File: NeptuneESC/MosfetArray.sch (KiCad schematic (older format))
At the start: 24 parts, among them Q1 Q_NPN_BCE, Q2 Q_NPN_BCE, Q3 Q_NPN_BCE

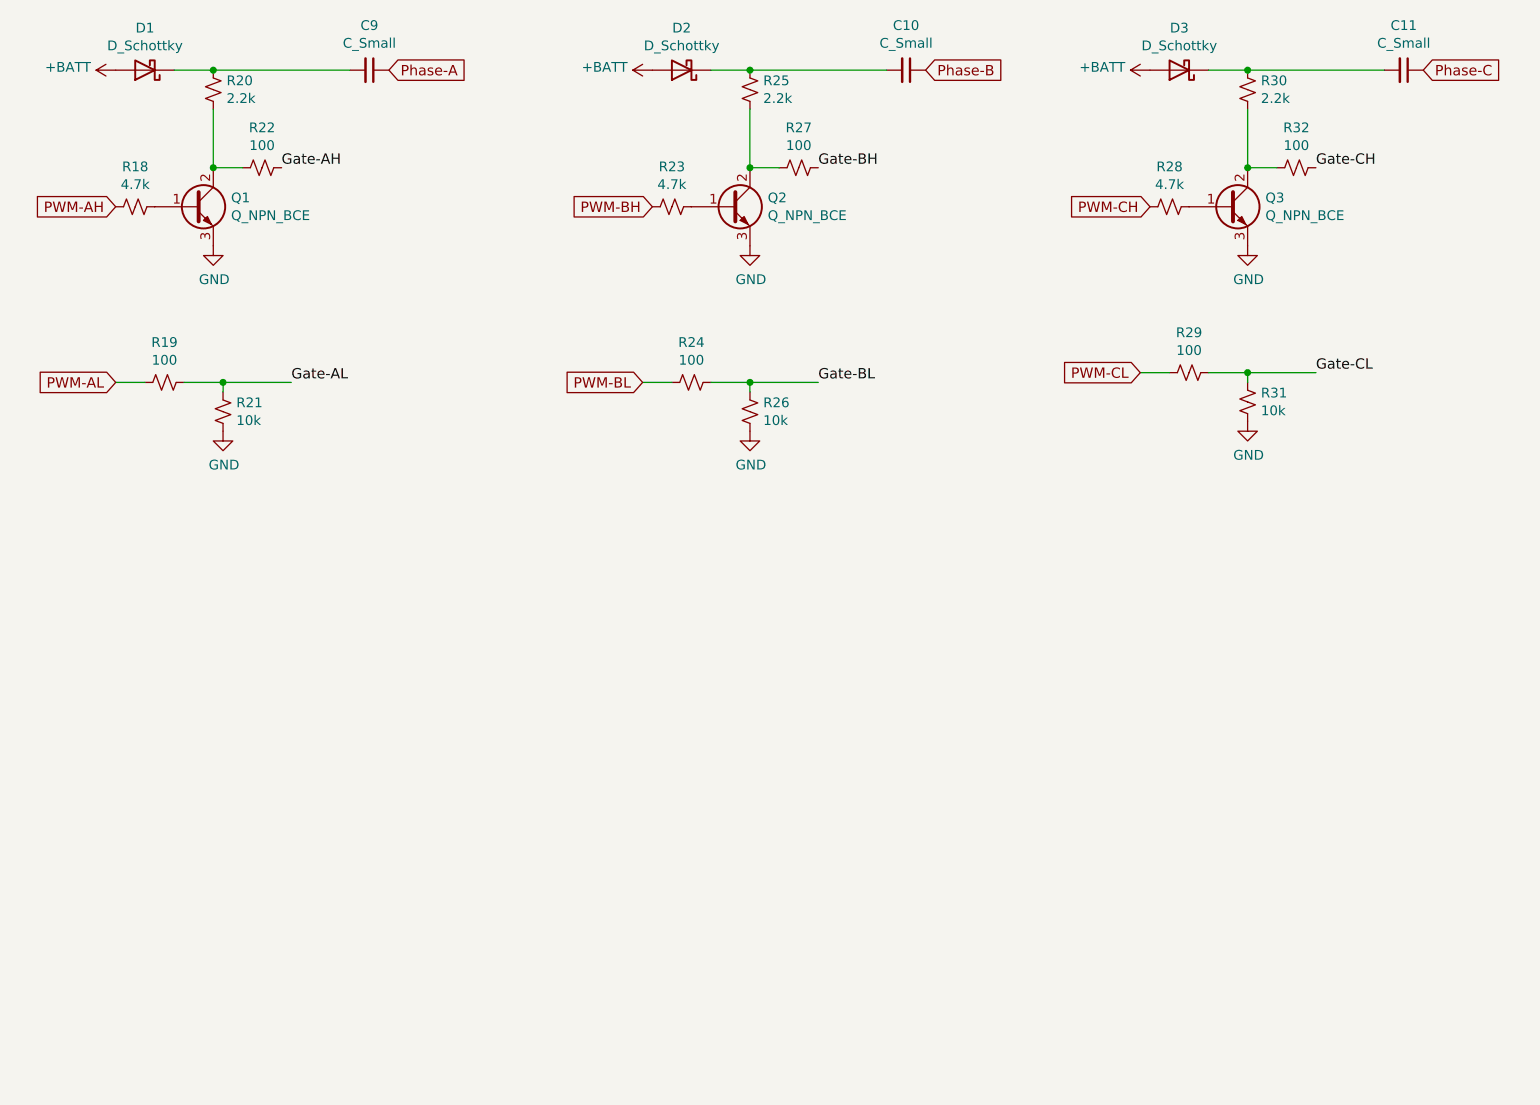
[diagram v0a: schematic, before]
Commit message: Innitial layout
Need to add motor pads
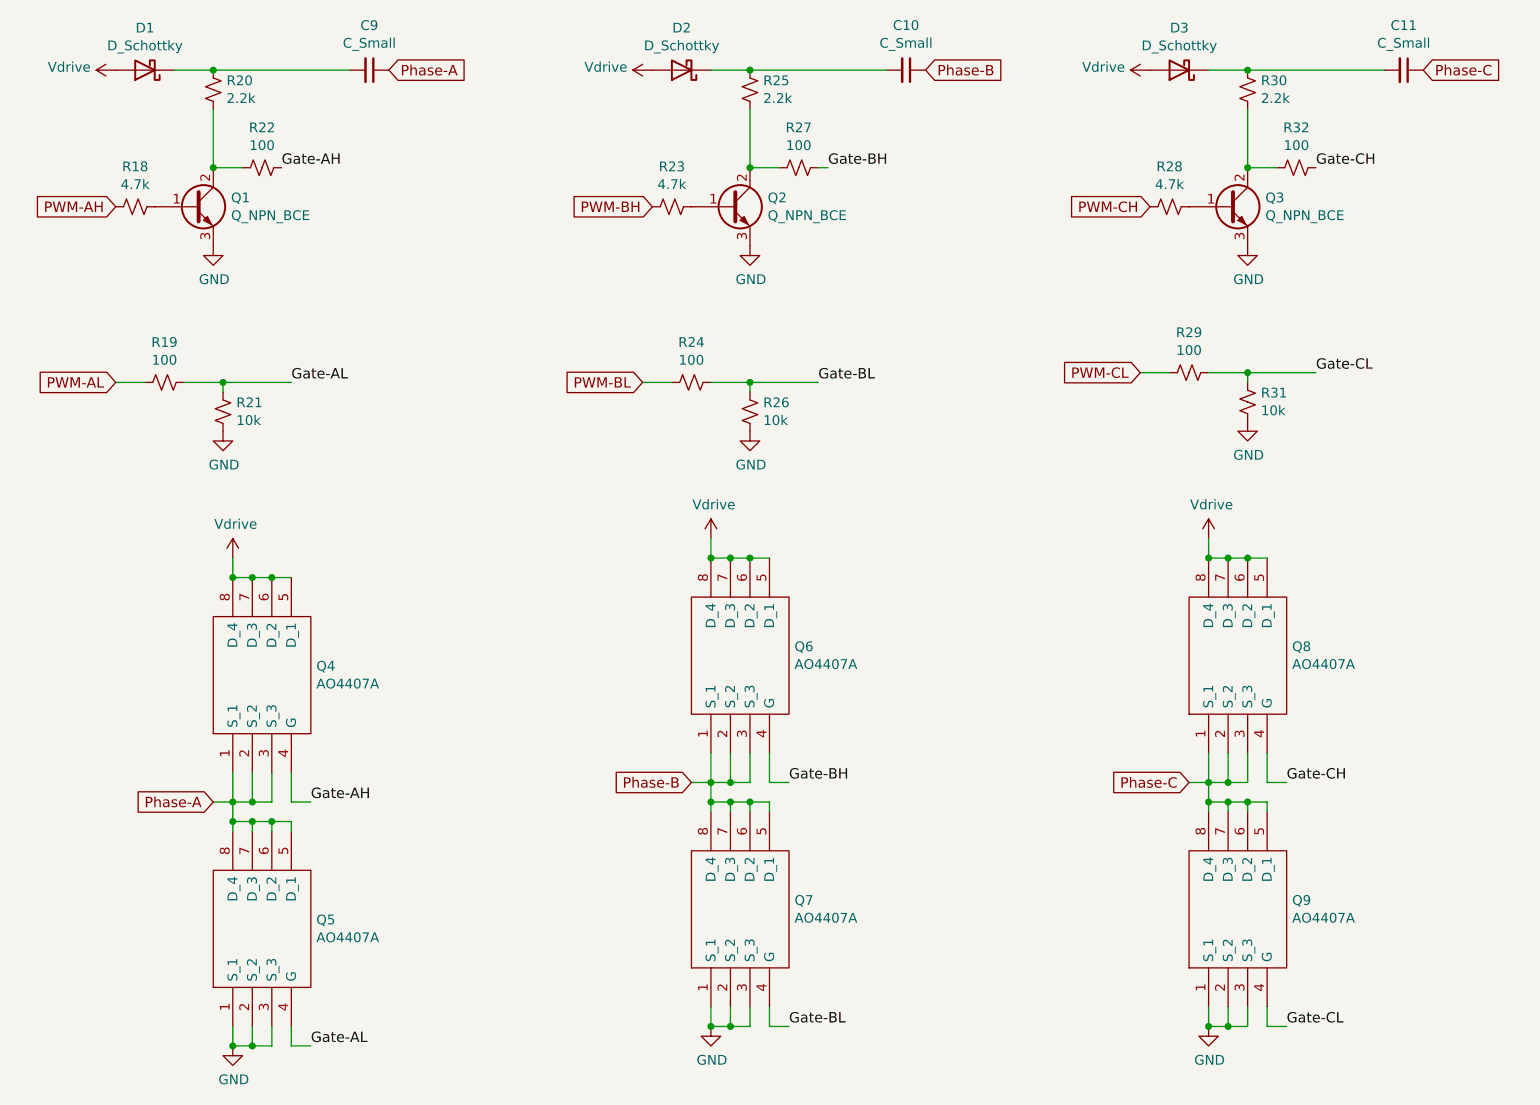
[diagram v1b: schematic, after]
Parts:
- added Q4, Q5, Q6, Q7, Q8, Q9: AO4407A, Used libraries:SOIC127P600X175-8N, symbol AO4407A:AO4407A
- C10, C11, C9: footprint (none) -> Capacitor_SMD:C_0402_1005Metric
- D1, D2, D3: footprint (none) -> Diode_SMD:D_SOD-123; JLCPCB (none) -> C8598
- Q1, Q2, Q3: footprint (none) -> Package_TO_SOT_SMD:SOT-23; JLCPCB (none) -> C2150
- R18, R23, R28: footprint (none) -> Resistor_SMD:R_0402_1005Metric; JLCPCB (none) -> C25900
- R19, R22, R24, R27, R29, R32: footprint (none) -> Resistor_SMD:R_0402_1005Metric; JLCPCB (none) -> C25741
- R20, R25, R30: footprint (none) -> Resistor_SMD:R_0402_1005Metric; JLCPCB (none) -> C25879
- R21, R26: footprint (none) -> Resistor_SMD:R_0402_1005Metric; JLCPCB (none) -> C25744
- R31: footprint (none) -> Resistor_SMD:R_0402_1005Metric
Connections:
- net GND: now also Q5.1 (S_1), Q5.2 (S_2), Q5.3 (S_3), Q7.1 (S_1), Q7.2 (S_2), Q7.3 (S_3), Q9.1 (S_1), Q9.2 (S_2), Q9.3 (S_3)
- net Gate-AH: now also Q4.4 (G)
- net Gate-AL: now also Q5.4 (G)
- net Gate-BH: now also Q6.4 (G)
- net Gate-BL: now also Q7.4 (G)
- net Gate-CH: now also Q8.4 (G)
- net Gate-CL: now also Q9.4 (G)
- net Phase-A: now also Q4.1 (S_1), Q4.2 (S_2), Q4.3 (S_3), Q5.5 (D_1), Q5.6 (D_2), Q5.7 (D_3), Q5.8 (D_4)
- net Phase-B: now also Q6.1 (S_1), Q6.2 (S_2), Q6.3 (S_3), Q7.5 (D_1), Q7.6 (D_2), Q7.7 (D_3), Q7.8 (D_4)
- net Phase-C: now also Q8.1 (S_1), Q8.2 (S_2), Q8.3 (S_3), Q9.5 (D_1), Q9.6 (D_2), Q9.7 (D_3), Q9.8 (D_4)
- net +BATT renamed Vdrive
- net Vdrive: now also Q4.5 (D_1), Q4.6 (D_2), Q4.7 (D_3), Q4.8 (D_4), Q6.5 (D_1), Q6.6 (D_2), Q6.7 (D_3), Q6.8 (D_4), Q8.5 (D_1), Q8.6 (D_2), Q8.7 (D_3), Q8.8 (D_4)
